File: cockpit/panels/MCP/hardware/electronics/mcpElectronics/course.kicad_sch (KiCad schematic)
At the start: 6 parts

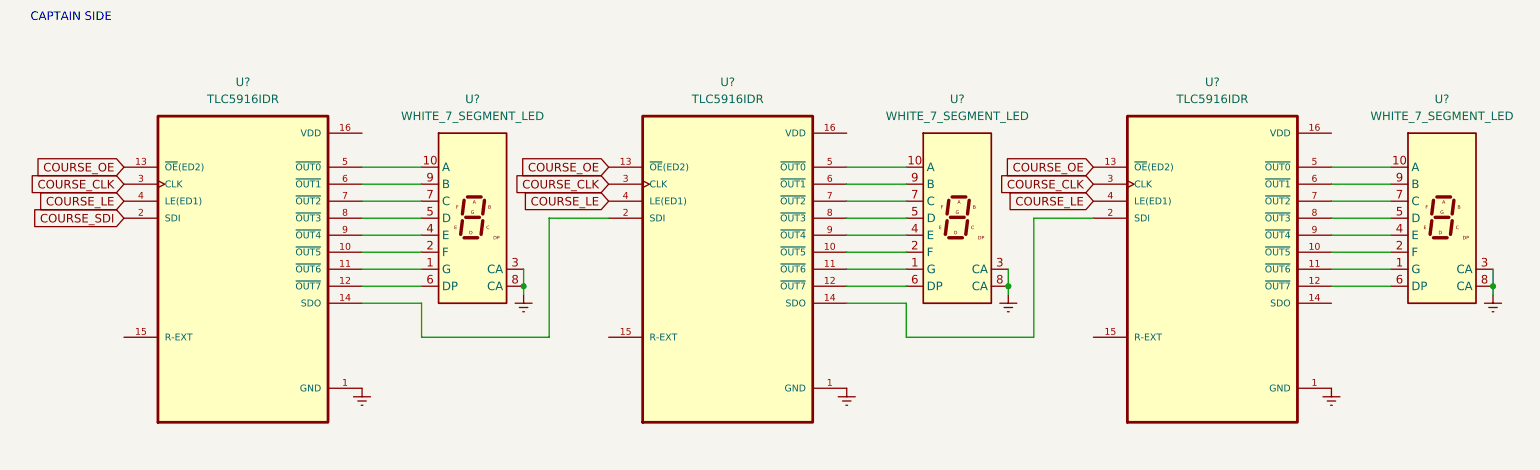
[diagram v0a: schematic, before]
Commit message: add more course display circuitry
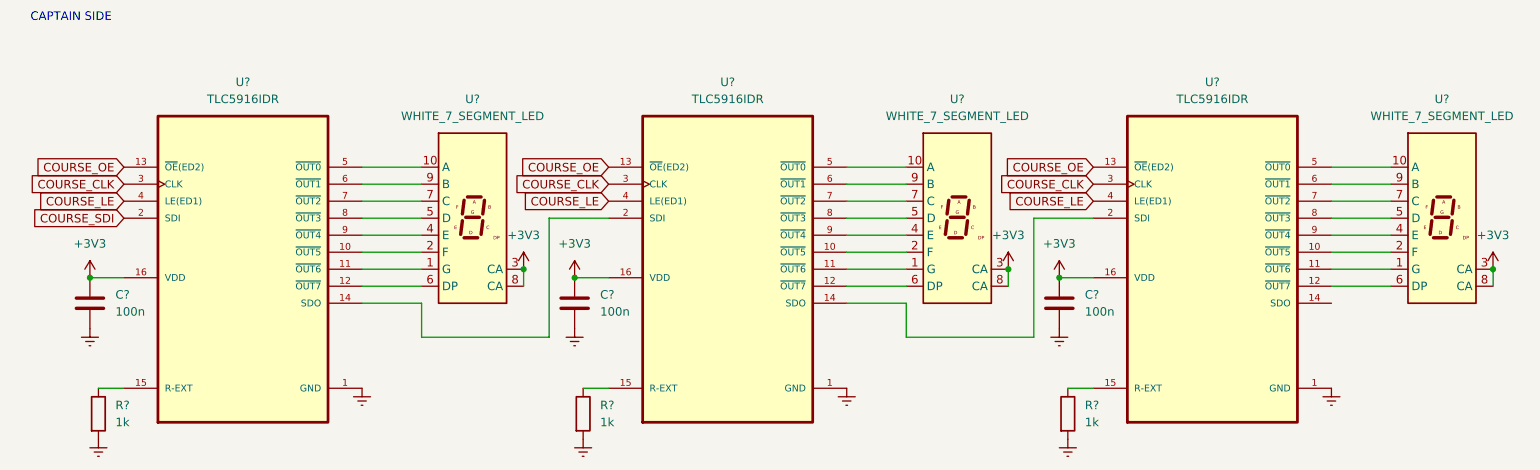
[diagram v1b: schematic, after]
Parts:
- removed U? (x2): TLC5916IDR, TLC5916IDR:SOIC127P600X175-16N, symbol TLC5916IDR:TLC5916IDR
- added C? (x3): 100n, symbol Device:C
- added R? (x3): 1k, symbol Device:R
- added U? (x2): TLC5916IDR, TLC5916IDR:SOIC127P600X175-16N, symbol TLC5916IDR:TLC5916IDR
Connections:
- net COURSE_CLK: now also U?.3 (CLK), U?.3 (CLK)
- net COURSE_LE: now also U?.4 (LE(ED1)), U?.4 (LE(ED1))
- net COURSE_OE: now also U?.13 (~{OE}(ED2)), U?.13 (~{OE}(ED2))
- net Earth: now also C?.2, C?.2, C?.2, R?.2, R?.2, R?.2, U?.1 (GND), U?.1 (GND); no longer U?.3 (CA), U?.3 (CA), U?.3 (CA), U?.8 (CA), U?.8 (CA), U?.8 (CA)
- net at U?.1 (G): now also U?.11 (~{OUT6}) (x2)
- net at U?.10 (A): now also U?.5 (~{OUT0}) (x2)
- net at U?.2 (F): now also U?.10 (~{OUT5}) (x2)
- net at U?.4 (E): now also U?.9 (~{OUT4}) (x2)
- net at U?.5 (D): now also U?.8 (~{OUT3}) (x2)
- net at U?.6 (DP): now also U?.12 (~{OUT7}) (x2)
- net at U?.7 (C): now also U?.7 (~{OUT2}) (x2)
- net at U?.9 (B): now also U?.6 (~{OUT1}) (x2)
- net at U?.14 (SDO): now also U?.2 (SDI)
- net at U?.15 (R-EXT): now also R?.1
- net +3V3: now reaches U?.16 (VDD)
- net +3V3: now also U?.3 (CA), U?.3 (CA), U?.3 (CA), U?.8 (CA), U?.8 (CA), U?.8 (CA), C?.1, C?.1, C?.1, U?.16 (VDD), U?.16 (VDD)
- new net: U?.14 (SDO), U?.2 (SDI)
- new net: R?.1, U?.15 (R-EXT) (x2)

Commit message: add electronics
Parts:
- added C? (x3): 100n, symbol Device:C
- added R? (x3): 1k, symbol Device:R
- added SW?: First Officer Course Knob, symbol Device:RotaryEncoder
- added SW?: Captain Course Knob, symbol Device:RotaryEncoder
- added U? (x3): WHITE_7_SEGMENT_LED, Display_7Segment:Sx39-1xxxxx, symbol Display_Character:SA39-11EWA
- added U? (x3): TLC5916IDR, TLC5916IDR:SOIC127P600X175-16N, symbol TLC5916IDR:TLC5916IDR
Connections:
- net +3V3: now also C?.1, C?.1, C?.1, U?.16 (VDD), U?.16 (VDD), U?.16 (VDD), U?.3 (CA), U?.3 (CA), U?.3 (CA), U?.8 (CA), U?.8 (CA), U?.8 (CA)
- net Earth: now also C?.2, C?.2, C?.2, R?.2, R?.2, R?.2, SW?.C, SW?.C, U?.1 (GND), U?.1 (GND), U?.1 (GND)
- net at U?.12 (~{OUT7}): no longer U?.6 (DP) (x2)
- net at U?.6 (DP): no longer U?.12 (~{OUT7})
- net COURSE_CLK renamed COURSE_CA_CLK
- net COURSE_LE renamed COURSE_CA_LE
- net COURSE_OE renamed COURSE_CA_OE
- net COURSE_SDI renamed COURSE_CA_SDI
- new net: U?.1 (G), U?.11 (~{OUT6}) (x3)
- new net: U?.10 (A), U?.5 (~{OUT0}) (x3)
- new net: U?.10 (~{OUT5}), U?.2 (F) (x3)
- new net: U?.4 (E), U?.9 (~{OUT4}) (x3)
- new net: U?.5 (D), U?.8 (~{OUT3}) (x3)
- new net: U?.7 (C), U?.7 (~{OUT2}) (x3)
- new net: U?.6 (~{OUT1}), U?.9 (B) (x3)
- new net: R?.1, U?.15 (R-EXT) (x3)
- new net: U?.14 (SDO), U?.2 (SDI) (x2)
- new net COURSE_CA_DEC: SW?.A
- new net COURSE_CA_INC: SW?.B
- new net COURSE_FO_CLK: U?.3 (CLK), U?.3 (CLK), U?.3 (CLK)
- new net COURSE_FO_DEC: SW?.A
- new net COURSE_FO_INC: SW?.B
- new net COURSE_FO_LE: U?.4 (LE(ED1)), U?.4 (LE(ED1)), U?.4 (LE(ED1))
- new net COURSE_FO_OE: U?.13 (~{OE}(ED2)), U?.13 (~{OE}(ED2)), U?.13 (~{OE}(ED2))
- new net COURSE_FO_SDI: U?.2 (SDI)
- no-connect marks 0 -> 14
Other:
- note added: "FIRST OFFICER SIDE"
- moved on the sheet: C?, R?, U?

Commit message: update
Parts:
- removed C? (x6): 100n, symbol Device:C
- removed R? (x6): 1k, symbol Device:R
- removed U? (x6): TLC5916IDR, TLC5916IDR:SOIC127P600X175-16N, symbol TLC5916IDR:TLC5916IDR
- removed U? (x6): WHITE_7_SEGMENT_LED, Display_7Segment:Sx39-1xxxxx, symbol Display_Character:SA39-11EWA
- added C3 (x6): 100n, Capacitor_SMD:C_0402_1005Metric, symbol Device:C
- added J18, J19, J20, J21, J22, J23: WHITE_7_SEGMENT_LED, Connector_PinHeader_2.54mm:PinHeader_1x09_P2.54mm_Vertical, symbol Connector:Conn_01x09_Pin
- added R138 (x4): 4k7, Resistor_SMD:R_0402_1005Metric, symbol Device:R
- SW2, SW3: renamed from SW?; footprint (none) -> Rotary_Encoder:RotaryEncoder_Bourns_Vertical_PEC12R-3x17F-Nxxxx
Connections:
- net +3V3: now also R138.1, R138.1, R138.1, R138.1
- net COURSE_CA_DEC: now also R138.2
- net COURSE_CA_INC: now also R138.2
- net COURSE_FO_DEC: now also R138.2
- net COURSE_FO_INC: now also R138.2
- net Earth: now also C3.2, C3.2, C3.2, C3.2, C3.2, C3.2
- new net LEDS_ANODE_3: C3.1, J18.8 (Pin_8), J18.9 (Pin_9)
- new net LEDS_ANODE_4: C3.1, J19.8 (Pin_8), J19.9 (Pin_9)
- new net LEDS_ANODE_5: C3.1, J20.8 (Pin_8), J20.9 (Pin_9)
- new net LEDS_ANODE_6: C3.1, J21.8 (Pin_8), J21.9 (Pin_9)
- new net LEDS_ANODE_7: C3.1, J22.8 (Pin_8), J22.9 (Pin_9)
- new net LEDS_ANODE_8: C3.1, J23.8 (Pin_8), J23.9 (Pin_9)
- new net LEDS_SEGMENTS_ROW_A: J18.1 (Pin_1), J19.1 (Pin_1), J20.1 (Pin_1), J21.1 (Pin_1), J22.1 (Pin_1), J23.1 (Pin_1)
- new net LEDS_SEGMENTS_ROW_B: J18.2 (Pin_2), J19.2 (Pin_2), J20.2 (Pin_2), J21.2 (Pin_2), J22.2 (Pin_2), J23.2 (Pin_2)
- new net LEDS_SEGMENTS_ROW_C: J18.3 (Pin_3), J19.3 (Pin_3), J20.3 (Pin_3), J21.3 (Pin_3), J22.3 (Pin_3), J23.3 (Pin_3)
- new net LEDS_SEGMENTS_ROW_D: J18.4 (Pin_4), J19.4 (Pin_4), J20.4 (Pin_4), J21.4 (Pin_4), J22.4 (Pin_4), J23.4 (Pin_4)
- new net LEDS_SEGMENTS_ROW_E: J18.5 (Pin_5), J19.5 (Pin_5), J20.5 (Pin_5), J21.5 (Pin_5), J22.5 (Pin_5), J23.5 (Pin_5)
- new net LEDS_SEGMENTS_ROW_F: J18.6 (Pin_6), J19.6 (Pin_6), J20.6 (Pin_6), J21.6 (Pin_6), J22.6 (Pin_6), J23.6 (Pin_6)
- new net LEDS_SEGMENTS_ROW_G: J18.7 (Pin_7), J19.7 (Pin_7), J20.7 (Pin_7), J21.7 (Pin_7), J22.7 (Pin_7), J23.7 (Pin_7)
- no-connect marks 14 -> 0
